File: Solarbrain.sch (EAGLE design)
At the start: 50 parts, among them IC1 MCP73871, Q1 MOSFET-NCHANNELSMD, Q2 MOSFET-NCHANNELFDD8580, Q3 MOSFET-NCHANNELSMD, U1 ATMEGA128_SMD

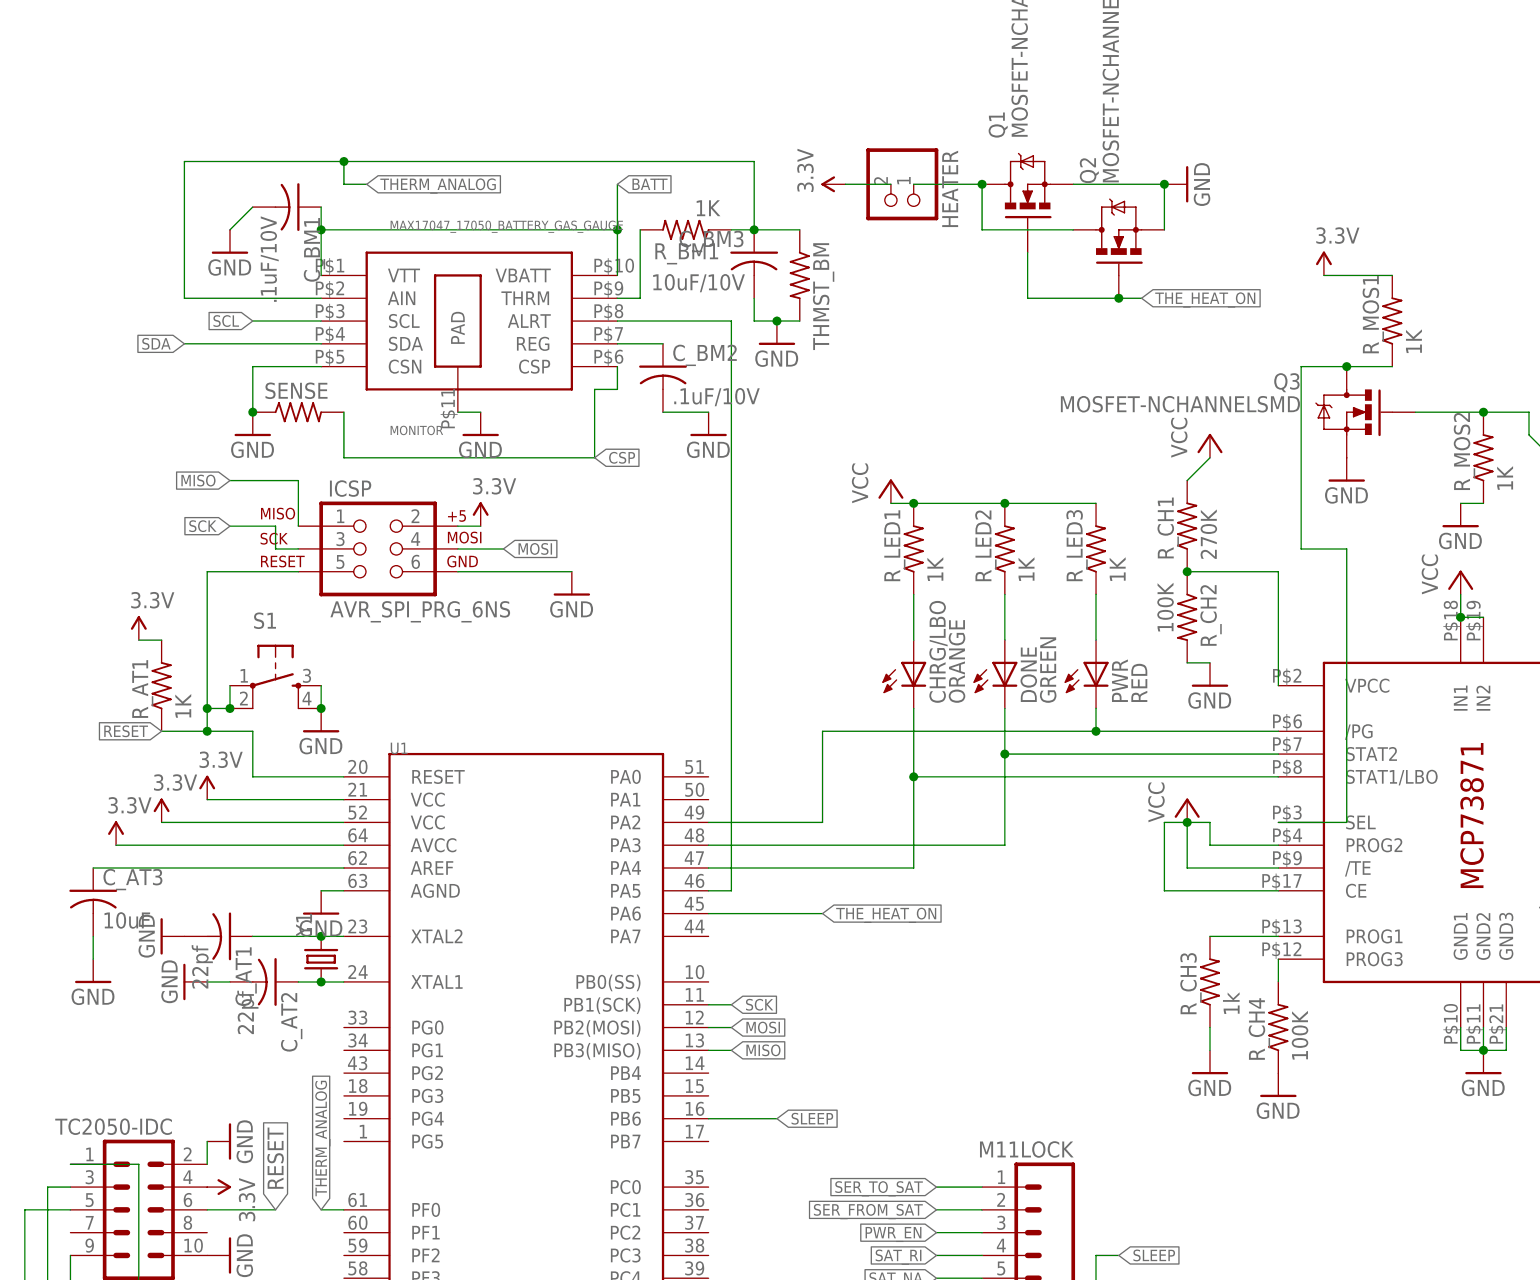
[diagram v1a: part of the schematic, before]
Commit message: major tweak list
issues addressed:

  * Atmega Circuit

   1. PWR_EN from sat connector net not connected to any I/O pin on
ATMega

   * Fuel Gauge Circuit

   1. VBATT (BATT) voltage sense trace for the MAX17047 should be a
Kelvin connection - needs to be split and routed separately from the
current carrying portion of trace to a point close to the battery input
   2. CVBATT (C_BM1) should be connected to VBATT's separate kelvin
line and PK-/CSP, not to main current carrying line and GND
   3. CREG (C_BM2) capacitor should be connected to PK-/CSP not GND.
(Figs 5 and 8 data sheet)
   4. THMST_BM should be connected to PK-/CSP- not GND (Fig 5 data
sheet)
   5. PAD should be connected to PK-/CSP not GND

    * JTAG Connector

   1. EAGLE footprint was provided from TC company with incorrect pin
mapping.  Actual numbers should be down-and-up not zig-zag-across.
Need to fix library footprint and re-route traces, for reference, the
TC2050-IDC data sheet is correctly numbered in all views.

    * PCB layout general

   1. All pads in copper pours need thermal cutouts
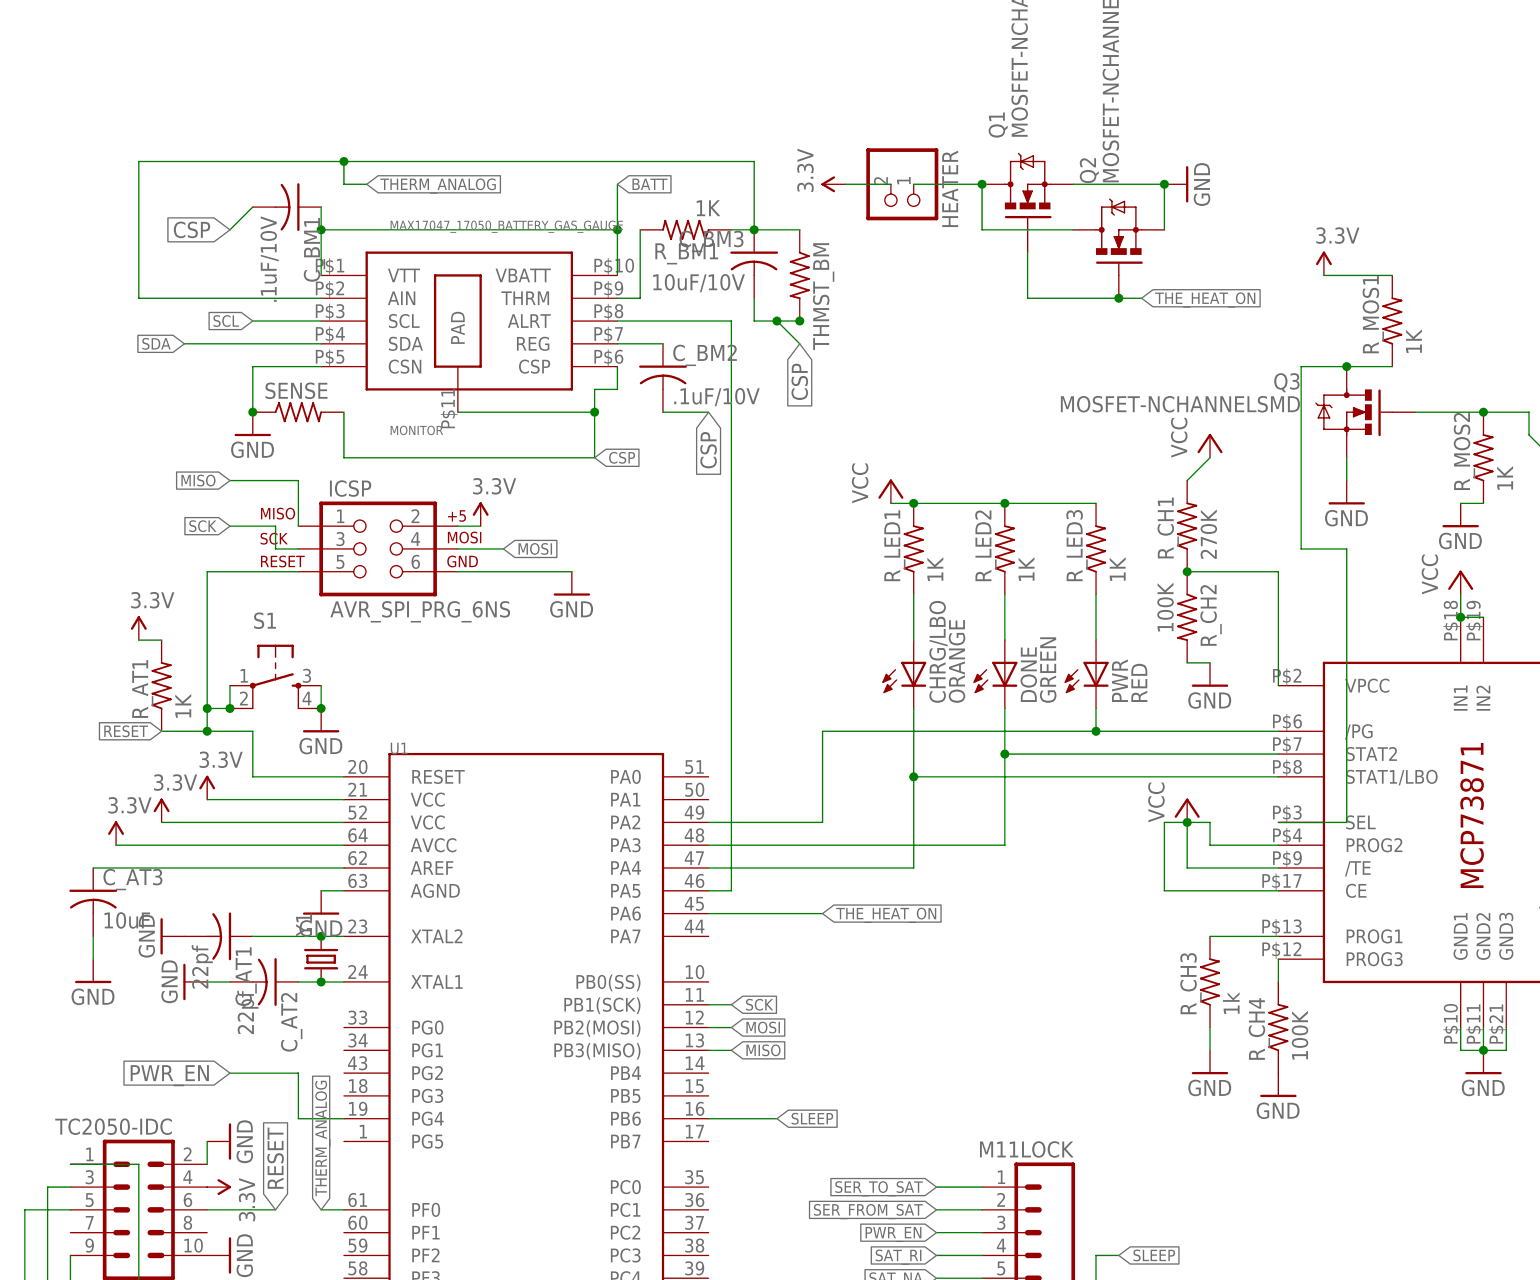
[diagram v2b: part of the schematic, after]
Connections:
- net CSP: now also C_BM1.2, C_BM2.2, C_BM3.2, MONITOR.PAD, THMST_BM.2
- net GND: no longer C_BM1.2, C_BM2.2, C_BM3.2, MONITOR.PAD, THMST_BM.2
- net PWR_EN: now also U1.PG4
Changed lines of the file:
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@@
 <part name="R_BM1" library="adafruit" deviceset="R-US_" device="R0603" value="1K"/>
 <part name="C_BM3" library="adafruit" deviceset="C-US" device="C0603" value="10uF/10V"/>
-<part name="GND19" library="supply1" deviceset="GND" device=""/>
 <part name="GND20" library="supply1" deviceset="GND" device=""/>
 <part name="C_BM2" library="adafruit" deviceset="C-US" device="C0603" value=".1uF/10V"/>
 <part name="C_BM1" library="adafruit" deviceset="C-US" device="C0603" value=".1uF/10V"/>
-<part name="GND21" library="supply1" deviceset="GND" device=""/>
-<part name="GND22" library="supply1" deviceset="GND" device=""/>
-<part name="GND23" library="supply1" deviceset="GND" device=""/>
 <part name="P+13" library="SparkFun2011" deviceset="3.3V" device=""/>
 <part name="GND29" library="supply1" deviceset="GND" device=""/>
@@
 <instance part="D1" gate="G$1" x="205.74" y="137.16"/>
 <instance part="Q3" gate="G$1" x="157.48" y="142.24" rot="MR0"/>
-<instance part="GND26" gate="1" x="157.48" y="134.62"/>
+<instance part="GND26" gate="1" x="157.48" y="132.08"/>
 <instance part="R_MOS1" gate="G$1" x="162.56" y="152.4" rot="R90"/>
 <instance part="P+12" gate="G$1" x="154.94" y="157.48"/>
@@
 <instance part="R_BM1" gate="G$1" x="83.82" y="162.56" rot="R180"/>
 <instance part="C_BM3" gate="G$1" x="91.44" y="160.02" rot="MR0"/>
-<instance part="GND19" gate="1" x="93.98" y="149.86"/>
 <instance part="GND20" gate="1" x="195.58" y="144.78" rot="R90"/>
 <instance part="C_BM2" gate="G$1" x="81.28" y="147.32"/>
 <instance part="C_BM1" gate="G$1" x="40.64" y="165.1" rot="R270"/>
-<instance part="GND21" gate="1" x="33.02" y="160.02"/>
-<instance part="GND22" gate="1" x="86.36" y="139.7"/>
-<instance part="GND23" gate="1" x="60.96" y="139.7"/>
 <instance part="P+13" gate="G$1" x="101.6" y="167.64" rot="R90"/>
 <instance part="GND29" gate="1" x="139.7" y="167.64" rot="R90"/>
@@
 <pinref part="Q3" gate="G$1" pin="S"/>
 <pinref part="GND26" gate="1" pin="GND"/>
+<wire x1="157.48" y1="134.62" x2="157.48" y2="137.16" width="0.1524" layer="91"/>
 </segment>
 <segment>
@@
 </segment>
 <segment>
-<pinref part="C_BM3" gate="G$1" pin="2"/>
-<wire x1="91.44" y1="154.94" x2="91.44" y2="152.4" width="0.1524" layer="91"/>
-<pinref part="THMST_BM" gate="G$1" pin="2"/>
-<wire x1="91.44" y1="152.4" x2="93.98" y2="152.4" width="0.1524" layer="91"/>
-<pinref part="GND19" gate="1" pin="GND"/>
-<wire x1="93.98" y1="152.4" x2="96.52" y2="152.4" width="0.1524" layer="91"/>
-<junction x="93.98" y="152.4"/>
-</segment>
-<segment>
 <pinref part="FTDI" gate="G$1" pin="6"/>
 <pinref part="GND20" gate="1" pin="GND"/>
 <wire x1="193.04" y1="142.24" x2="193.04" y2="144.78" width="0.1524" layer="91"/>
-</segment>
-<segment>
-<pinref part="C_BM1" gate="G$1" pin="2"/>
-<pinref part="GND21" gate="1" pin="GND"/>
-<wire x1="35.56" y1="165.1" x2="33.02" y2="162.56" width="0.1524" layer="91"/>
-</segment>
-<segment>
-<pinref part="C_BM2" gate="G$1" pin="2"/>
-<pinref part="GND22" gate="1" pin="GND"/>
-<wire x1="86.36" y1="142.24" x2="81.28" y2="142.24" width="0.1524" layer="91"/>
-</segment>
-<segment>
-<pinref part="MONITOR" gate="G$1" pin="PAD"/>
-<pinref part="GND23" gate="1" pin="GND"/>
-<wire x1="60.96" y1="142.24" x2="58.42" y2="142.24" width="0.1524" layer="91"/>
 </segment>
 <segment>
@@
 <wire x1="91.44" y1="162.56" x2="91.44" y2="170.18" width="0.1524" layer="91"/>
 <wire x1="91.44" y1="170.18" x2="45.72" y2="170.18" width="0.1524" layer="91"/>
-<wire x1="45.72" y1="170.18" x2="27.94" y2="170.18" width="0.1524" layer="91"/>
-<wire x1="27.94" y1="170.18" x2="27.94" y2="154.94" width="0.1524" layer="91"/>
+<wire x1="45.72" y1="170.18" x2="22.86" y2="170.18" width="0.1524" layer="91"/>
+<wire x1="22.86" y1="170.18" x2="22.86" y2="154.94" width="0.1524" layer="91"/>
 <pinref part="MONITOR" gate="G$1" pin="AIN"/>
-<wire x1="27.94" y1="154.94" x2="43.18" y2="154.94" width="0.1524" layer="91"/>
+<wire x1="22.86" y1="154.94" x2="43.18" y2="154.94" width="0.1524" layer="91"/>
 <wire x1="45.72" y1="170.18" x2="45.72" y2="167.64" width="0.1524" layer="91"/>
 <junction x="45.72" y="170.18"/>
@@
 <wire x1="45.72" y1="142.24" x2="45.72" y2="137.16" width="0.1524" layer="91"/>
 <wire x1="45.72" y1="137.16" x2="73.66" y2="137.16" width="0.1524" layer="91"/>
-<wire x1="73.66" y1="137.16" x2="73.66" y2="144.78" width="0.1524" layer="91"/>
+<wire x1="73.66" y1="137.16" x2="73.66" y2="142.24" width="0.1524" layer="91"/>
+<wire x1="73.66" y1="142.24" x2="73.66" y2="144.78" width="0.1524" layer="91"/>
 <wire x1="73.66" y1="144.78" x2="76.2" y2="144.78" width="0.1524" layer="91"/>
 <label x="73.66" y="137.16" size="1.27" layer="95" xref="yes"/>
+<pinref part="MONITOR" gate="G$1" pin="PAD"/>
+<wire x1="58.42" y1="142.24" x2="73.66" y2="142.24" width="0.1524" layer="91"/>
+<junction x="73.66" y="142.24"/>
 </segment>
 <segment>
@@
 <pinref part="BATT" gate="G$1" pin="1"/>
 <label x="233.68" y="91.44" size="1.27" layer="95" rot="R180" xref="yes"/>
+</segment>
+<segment>
+<pinref part="C_BM1" gate="G$1" pin="2"/>
+<wire x1="35.56" y1="165.1" x2="33.02" y2="162.56" width="0.1524" layer="91"/>
+<label x="33.02" y="162.56" size="1.778" layer="95" rot="R180" xref="yes"/>
+</segment>
+<segment>
+<pinref part="C_BM3" gate="G$1" pin="2"/>
+<wire x1="91.44" y1="154.94" x2="91.44" y2="152.4" width="0.1524" layer="91"/>
+<wire x1="91.44" y1="152.4" x2="93.98" y2="152.4" width="0.1524" layer="91"/>
+<pinref part="THMST_BM" gate="G$1" pin="2"/>
+<junction x="96.52" y="152.4"/>
+<wire x1="96.52" y1="152.4" x2="93.98" y2="152.4" width="0.1524" layer="91"/>
+<junction x="93.98" y="152.4"/>
+<wire x1="93.98" y1="152.4" x2="96.52" y2="149.86" width="0.1524" layer="91"/>
+<label x="96.52" y="149.86" size="1.778" layer="95" rot="R270" xref="yes"/>
+</segment>
+<segment>
+<pinref part="C_BM2" gate="G$1" pin="2"/>
+<wire x1="86.36" y1="142.24" x2="81.28" y2="142.24" width="0.1524" layer="91"/>
+<label x="86.36" y="142.24" size="1.778" layer="95" rot="R270" xref="yes"/>
 </segment>
 </net>
@@
 <label x="111.76" y="50.8" size="1.27" layer="95" rot="R180" xref="yes"/>
 </segment>
-</net>
+<segment>
+<pinref part="U1" gate="G$1" pin="PG4"/>
+<wire x1="45.72" y1="63.5" x2="40.64" y2="63.5" width="0.1524" layer="91"/>
+<wire x1="40.64" y1="63.5" x2="40.64" y2="68.58" width="0.1524" layer="91"/>
+<wire x1="40.64" y1="68.58" x2="33.02" y2="68.58" width="0.1524" layer="91"/>
+<label x="33.02" y="68.58" size="1.778" layer="95" rot="R180" xref="yes"/>
+</segment>
+</net>
